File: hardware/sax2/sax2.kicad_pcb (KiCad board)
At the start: 4 copper layers, 80 x 34.5 mm, 105 parts, among them IC1401 MP3V5004GP, J101 Cortex, J102 DX07S016JA3, J1101 NE8FAH, J1301 2x05_Horizontal, SW101 SKSG, SW102 SKSG, U101 TPS78433QWDRBRQ1, U102 ATSAMD51J, U1101 THVD2442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

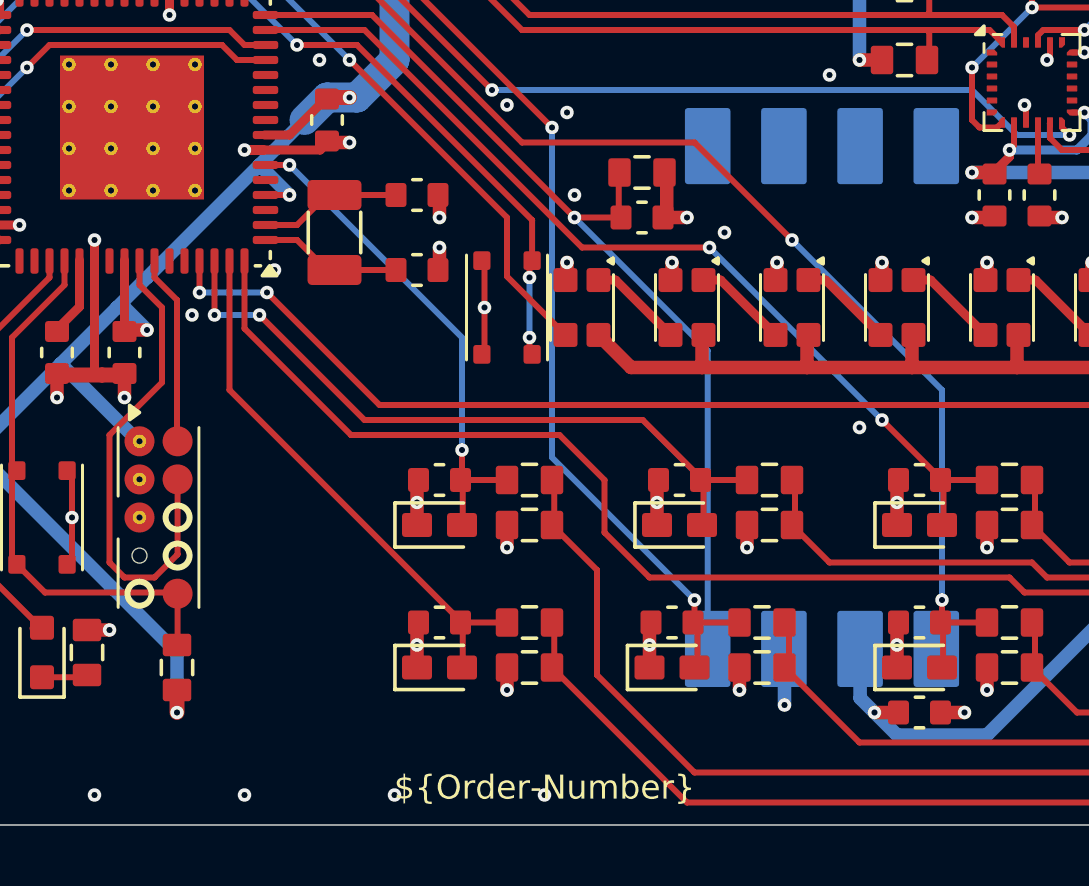
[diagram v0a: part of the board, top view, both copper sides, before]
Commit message: Replace Order_Number
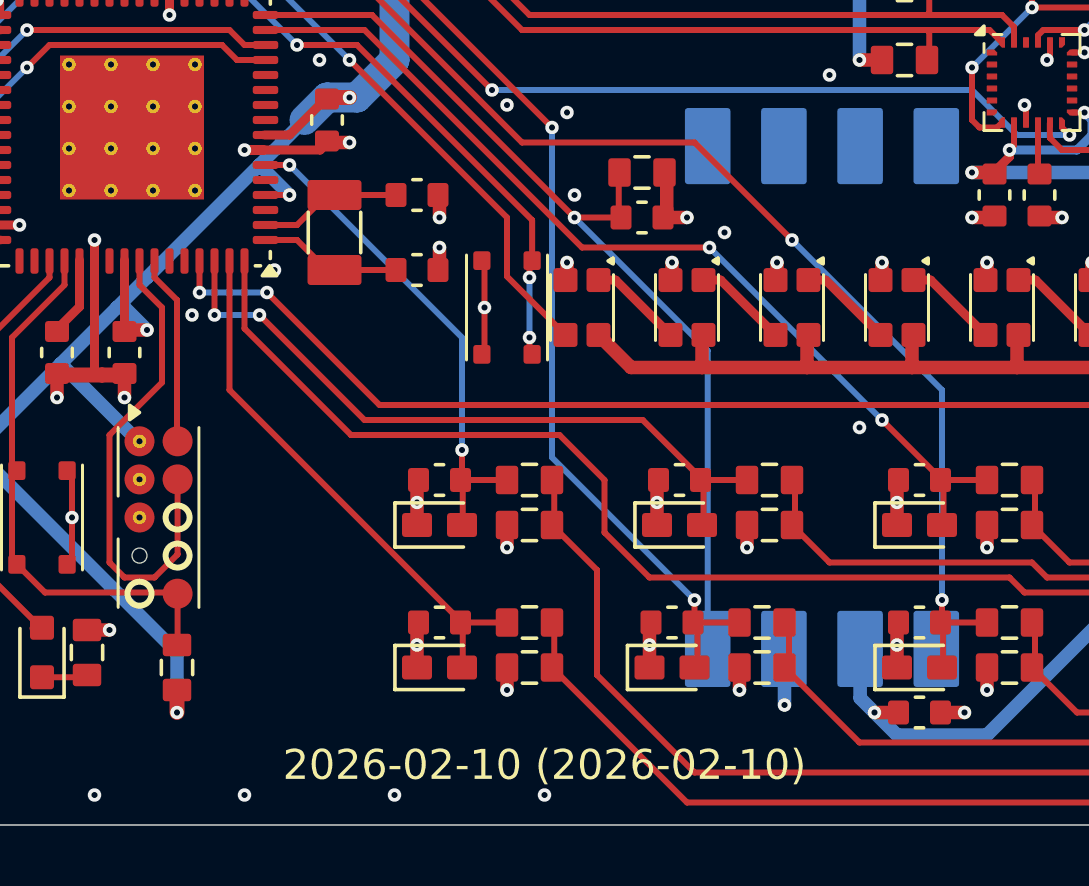
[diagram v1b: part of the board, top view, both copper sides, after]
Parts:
- H101: value MountingHole_2mm -> 2mm
- INFO101: value Order_Number -> ~; footprint V2_Production:Order_Number -> V2_Production:Revision
- moved INFO101 0.75 mm to (102.5, 115.5)
